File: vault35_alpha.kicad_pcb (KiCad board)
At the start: 2 copper layers, 209.7 x 76.4 mm, 132 parts, among them J1 AVR-ISP-6, SW1 SW_PUSH, SW2 RotaryEncoder_Switch, SW3 RotaryEncoder_Switch, SW4 RotaryEncoder_Switch, SW5 SW_PUSH, SW6 SW_PUSH, U1 SRV05-4, U2 ATmega32U4-M, X1 Crystal_GND24_Small

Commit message: Update
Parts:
- removed D_SPACE28, D_SPACE37: D, Diode_SMD:D_SOD-123
- removed K_SPACE49, K_SPACE52, K_SPACE53, K_SPACE54, K_SPACE55, K_SPACE56: KEYSW, MX_Only:MXOnly-1.25U-NoLED
- removed K_SPACE50, K_SPACE51: KEYSW, MX_Only:MXOnly-1.75U-NoLED
- removed K_SPACE57, K_SPACE58, K_SPACE59: KEYSW, MX_Only:MXOnly-3U-ReversedStabilizers-NoLED
- removed K_SPACE60, K_SPACE61: KEYSW, MX_Only:MXOnly-1.5U-NoLED
- removed OL2: OLED, kbd:OLED_v2
- removed REF**: 3U, MX_Only:MXOnly-3U-NoSwitch
- removed SW4: RotaryEncoder_Switch, encoder:RotaryEncoder_Alps_EC11E-Switch_Vertical_H20mm
- added C10: 2.2uF, Capacitor_SMD:C_0805_2012Metric_Pad1.18x1.45mm_HandSolder, B.Cu at (167.5, 75.4)
- added TP1: TPCLK, TestPoint:TestPoint_THTPad_1.0x1.0mm_Drill0.5mm, B.Cu at (164.3, 76.2)
- added TP2: TPVCC, TestPoint:TestPoint_THTPad_1.0x1.0mm_Drill0.5mm, B.Cu at (164.3, 82.5)
- added TP3: TPGND, TestPoint:TestPoint_THTPad_1.0x1.0mm_Drill0.5mm, B.Cu at (164.3, 79.4)
- added TP4: TPDATA, TestPoint:TestPoint_THTPad_1.0x1.0mm_Drill0.5mm, B.Cu at (164.3, 69.8)
- added TP5: TPRST, TestPoint:TestPoint_THTPad_1.0x1.0mm_Drill0.5mm, B.Cu at (164.3, 73.0)
- added UR6: 4.7k, Resistor_SMD:R_0805_2012Metric_Pad1.20x1.40mm_HandSolder, B.Cu at (167.5, 78.6)
- added UR7: 4.7k, Resistor_SMD:R_0805_2012Metric_Pad1.20x1.40mm_HandSolder, B.Cu at (167.5, 69.8)
- added UR8: 100k, Resistor_SMD:R_0805_2012Metric_Pad1.20x1.40mm_HandSolder, B.Cu at (167.5, 72.2)
- K_SPACE23, K_SPACE28, K_SPACE33, K_SPACE39: footprint MX_Only:MXOnly-1U-NoLED -> MX_Only:MXOnly-1.5U-NoLED
- K_SPACE34: footprint MX_Only:MXOnly-1.5U-NoLED -> MX_Only:MXOnly-1.25U-NoLED
- K_SPACE35, K_SPACE45: footprint MX_Only:MXOnly-1U-NoLED -> MX_Only:MXOnly-1.75U-NoLED
- K_SPACE36, K_SPACE37, K_SPACE38, K_SPACE41, K_SPACE42: footprint MX_Only:MXOnly-1U-NoLED -> MX_Only:MXOnly-1.25U-NoLED
- K_SPACE40: footprint MX_Only:MXOnly-1.5U-NoLED -> MX_Only:MXOnly-3U-ReversedStabilizers-NoSwitch
- K_SPACE43, K_SPACE44: footprint MX_Only:MXOnly-2U-ReversedStabilizers-NoLED -> MX_Only:MXOnly-1U-NoLED
- K_SPACE46: footprint MX_Only:MXOnly-1U-NoLED -> MX_Only:MXOnly-6U-Centered-ReversedStabilizers-NoLED
- K_SPACE47: footprint MX_Only:MXOnly-2.25U-ReversedStabilizers-NoLED -> MX_Only:MXOnly-1U-NoLED
- K_SPACE48: footprint MX_Only:MXOnly-2.75U-ReversedStabilizers-NoLED -> MX_Only:MXOnly-1U-NoLED
- moved K_SPACE42 111.9 mm to (221.5, 123.0)
- moved K_SPACE41 111.9 mm to (202.4, 123.0)
- moved K_SPACE47 69.1 mm to (200.0, 123.0)
- moved K_SPACE37 64.3 mm to (92.9, 123.0)
- moved K_SPACE45 64.3 mm to (140.5, 123.0)
- moved K_SPACE44 61.9 mm to (114.3, 123.0)
- moved K_SPACE40 61.9 mm to (157.2, 123.0)
- moved K_SPACE46 61.9 mm to (161.9, 123.0)
- moved K_SPACE36 59.5 mm to (197.6, 123.0)
- moved K_SPACE38 59.5 mm to (116.7, 123.0)
- moved K_SPACE35 54.8 mm to (173.8, 123.0)
- moved K_SPACE39 52.4 mm to (142.9, 123.0)
- moved K_SPACE43 47.6 mm to (90.5, 123.0)
- moved K_SPACE48 45.2 mm to (223.8, 123.0)
- moved K_SPACE28 23.8 mm to (171.4, 123.0)
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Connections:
- J1 pad 1: col3 -> row1
- J1 pad 4: row1 -> encA
- K_SPACE28 pad 1: col5 -> col6
- K_SPACE28 pad 2: Net-(D_SPACE28-Pad2) -> Net-(D_SPACE38-Pad2)
- K_SPACE34 pad 1: col2 -> col3
- K_SPACE34 pad 2: Net-(D_SPACE34-Pad2) -> Net-(D_SPACE35-Pad2)
- K_SPACE35 pad 1: col3 -> col6
- K_SPACE35 pad 2: Net-(D_SPACE35-Pad2) -> Net-(D_SPACE38-Pad2)
- K_SPACE36 pad 1: col4 -> col7
- K_SPACE36 pad 2: Net-(D_SPACE36-Pad2) -> Net-(D_SPACE39-Pad2)
- K_SPACE37 pad 1: col5 -> col2
- K_SPACE37 pad 2: Net-(D_SPACE37-Pad2) -> Net-(D_SPACE34-Pad2)
- K_SPACE38 pad 1: col6 -> col3
- K_SPACE38 pad 2: Net-(D_SPACE38-Pad2) -> Net-(D_SPACE35-Pad2)
- K_SPACE39 pad 1: col7 -> col4
- K_SPACE39 pad 2: Net-(D_SPACE39-Pad2) -> Net-(D_SPACE36-Pad2)
- K_SPACE41 pad 1: col2 -> col7
- K_SPACE41 pad 2: Net-(D_SPACE34-Pad2) -> Net-(D_SPACE39-Pad2)
- K_SPACE42 pad 1: col3 -> col8
- K_SPACE42 pad 2: Net-(D_SPACE35-Pad2) -> Net-(D_SPACE40-Pad2)
- K_SPACE43 pad 1: col4 -> col2
- K_SPACE43 pad 2: Net-(D_SPACE36-Pad2) -> Net-(D_SPACE34-Pad2)
- K_SPACE44 pad 1: col6 -> col3
- K_SPACE44 pad 2: Net-(D_SPACE38-Pad2) -> Net-(D_SPACE35-Pad2)
- K_SPACE45 pad 1: col7 -> col4
- K_SPACE45 pad 2: Net-(D_SPACE39-Pad2) -> Net-(D_SPACE36-Pad2)
- K_SPACE46 pad 1: col8 -> col6
- K_SPACE46 pad 2: Net-(D_SPACE40-Pad2) -> Net-(D_SPACE38-Pad2)
- K_SPACE47 pad 1: col4 -> col7
- K_SPACE47 pad 2: Net-(D_SPACE36-Pad2) -> Net-(D_SPACE39-Pad2)
- K_SPACE48 pad 1: col6 -> col8
- K_SPACE48 pad 2: Net-(D_SPACE38-Pad2) -> Net-(D_SPACE40-Pad2)
- U2 pad 10: row1 -> encA
- U2 pad 11: col3 -> row1
- U2 pad 20: col10 -> PD2
- U2 pad 21: col9 -> col5
- U2 pad 22: unconnected-(U2-Pad22) -> PD5
- U2 pad 25: col2 -> col10
- U2 pad 26: col8 -> col9
- U2 pad 27: col7 -> col8
- U2 pad 28: col6 -> col7
- U2 pad 29: encA -> col6
- U2 pad 30: encB -> col4
- U2 pad 31: col5 -> col3
- U2 pad 32: unconnected-(U2-Pad32) -> col2
- U2 pad 36: col1 -> unconnected-(U2-Pad36)
- U2 pad 37: row2 -> unconnected-(U2-Pad37)
- U2 pad 38: col0 -> row2
- U2 pad 41: unconnected-(U2-Pad41) -> col0
- U2 pad 8: unconnected-(U2-Pad8) -> col1
- U2 pad 9: col4 -> encB
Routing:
- net PD2: track 0.00 -> 120.9 mm, vias 0 -> 1
- net PD5: track 0.00 -> 116.4 mm, vias 0 -> 1
- net encB: track 130.8 -> 98.0 mm, vias 0 -> 2
- net col8: track 202.3 -> 230.7 mm
- net row3: track 231.5 -> 206.7 mm
- net col4: track 126.5 -> 150.4 mm
- net col7: track 180.5 -> 203.6 mm
- net encA: track 116.8 -> 94.7 mm, vias 2 -> 3
- net row0: track 250.1 -> 228.1 mm
- net D-: track 19.6 -> 39.1 mm
- net D+: track 17.5 -> 37.0 mm
- net col10: track 204.5 -> 221.1 mm, vias 0 -> 1
- net +5V: track 182.6 -> 166.0 mm
- net col2: track 90.8 -> 107.4 mm
- net col9: track 185.2 -> 200.2 mm, vias 0 -> 1
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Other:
- board text removed: "2"
- board text removed: "7"
- board text removed: "8"

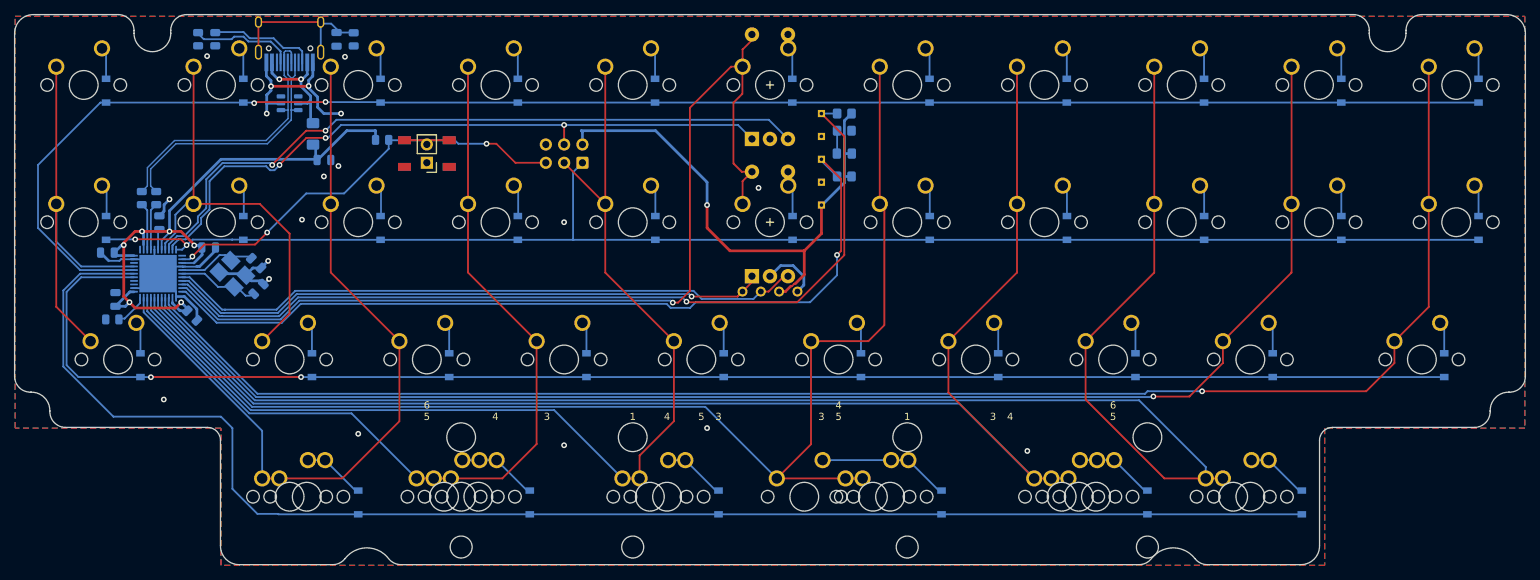
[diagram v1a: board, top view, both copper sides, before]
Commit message: update with TP, alpha stagger
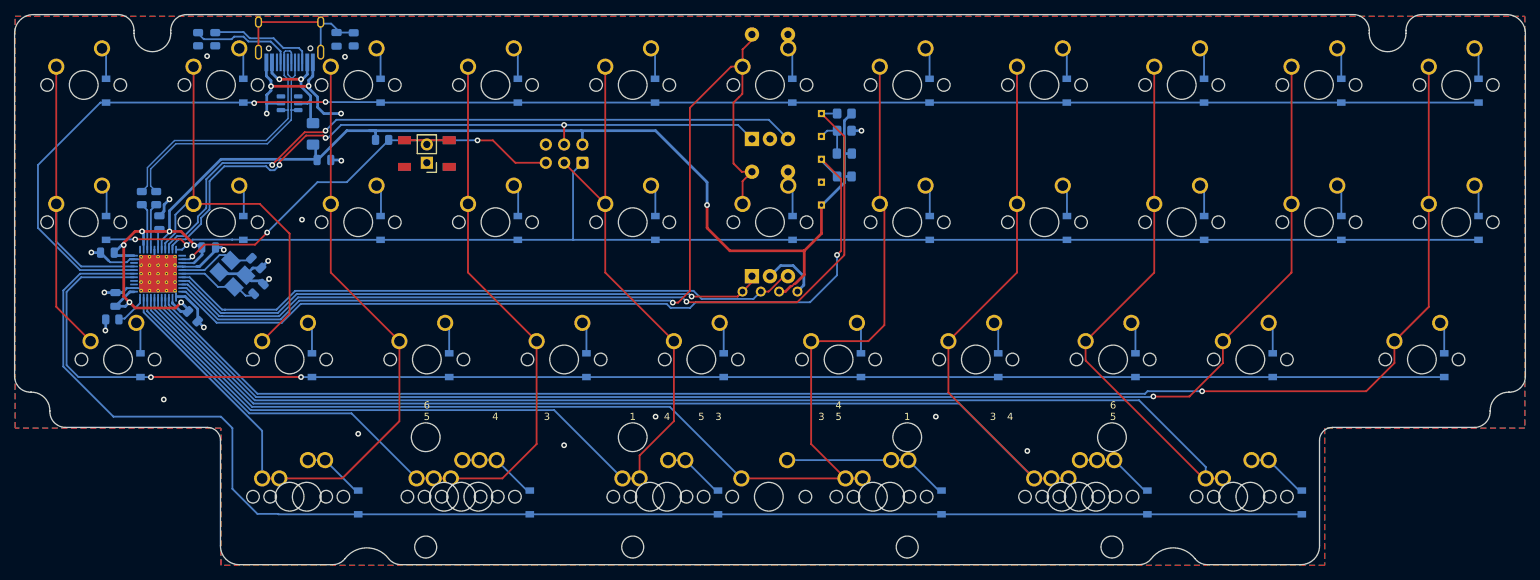
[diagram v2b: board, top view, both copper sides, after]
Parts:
- U2: footprint Package_DFN_QFN:QFN-44-1EP_7x7mm_P0.5mm_EP5.2x5.2mm -> Package_DFN_QFN:QFN-44-1EP_7x7mm_P0.5mm_EP5.2x5.2mm_ThermalVias
- moved K_SPACE46 4.92 mm to (157.0, 123.0)
- moved C5 0.15 mm to (77.1, 98.0)
- moved D_SPACE36 0.07 mm to (149.9, 123.8)
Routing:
- net +5V: track 166.0 -> 195.3 mm
- net GND: track 79.2 -> 92.1 mm, vias 19 -> 23
- net Net-(D_SPACE38-Pad2): track 17.9 -> 22.8 mm
- net col8: track 230.7 -> 227.6 mm
- net Net-(C10-Pad2): track 3.14 -> 5.64 mm
- net RST: track 66.5 -> 65.8 mm
